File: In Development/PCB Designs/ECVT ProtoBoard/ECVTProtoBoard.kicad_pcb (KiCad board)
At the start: 2 copper layers, 28 parts, among them J1 Motor Driver, J10 Conn_01x08, J11 5V, J12 Hall Effect, J13 Hall Effect, J14 External Power Switch, J15 Conn_01x08, J16 MotorDriver2, J18 3V3, J19 GND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

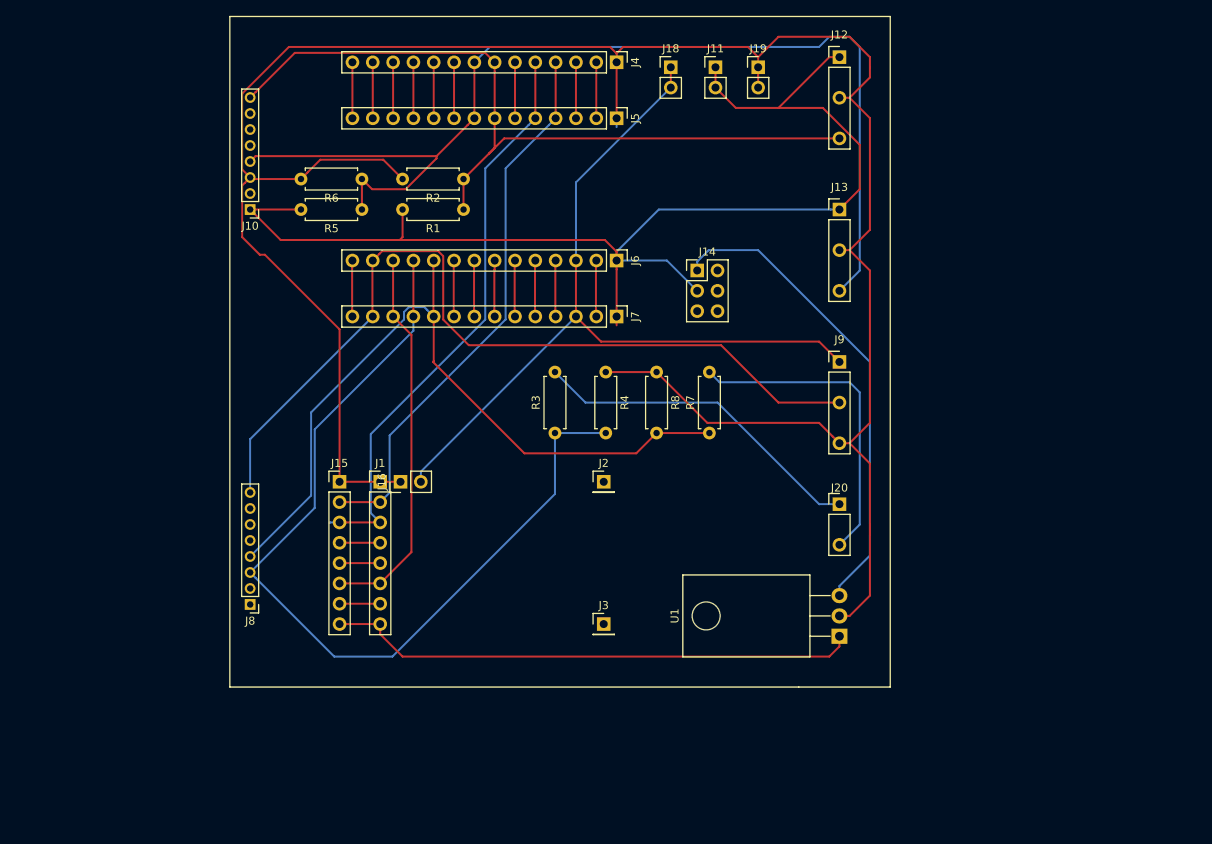
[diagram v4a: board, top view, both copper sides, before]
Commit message: Fixed edge cuts on DAQ PCB
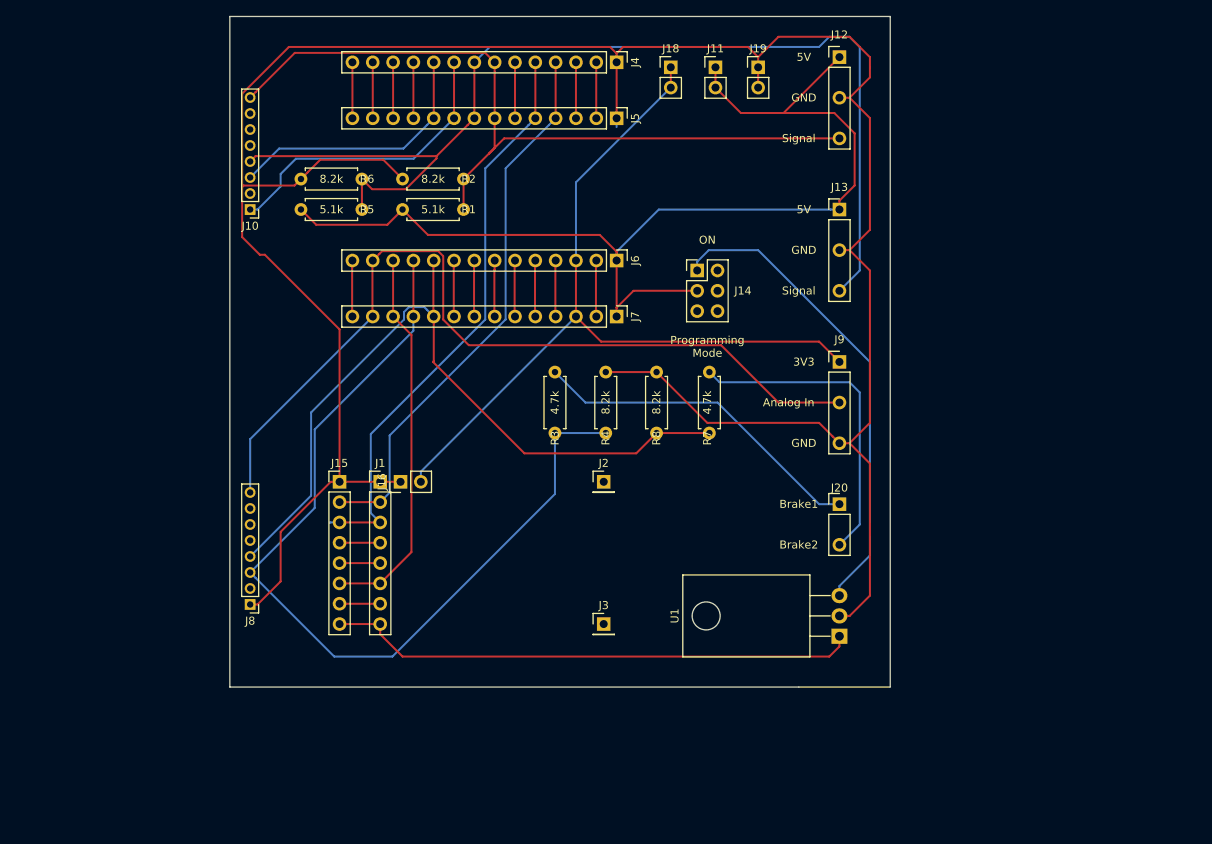
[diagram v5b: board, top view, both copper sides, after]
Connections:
- J10 pad 3: Net-(J1-Pad1) -> Net-(J10-Pad3)
- J11 pad 1: Net-(J10-Pad1) -> Net-(J11-Pad1)
- J11 pad 2: Net-(J10-Pad1) -> Net-(J11-Pad1)
- J12 pad 1: Net-(J10-Pad1) -> Net-(J11-Pad1)
- J13 pad 1: Net-(J10-Pad1) -> Net-(J11-Pad1)
- J14 pad 3: Net-(J10-Pad1) -> Net-(J11-Pad1)
- J4 pad 10: Net-(J4-Pad10) -> Net-(J10-Pad3)
- J4 pad 9: Net-(J4-Pad9) -> Net-(J10-Pad1)
- J5 pad 10: Net-(J4-Pad10) -> Net-(J10-Pad3)
- J5 pad 9: Net-(J4-Pad9) -> Net-(J10-Pad1)
- J6 pad 1: Net-(J10-Pad1) -> Net-(J11-Pad1)
- J7 pad 1: Net-(J10-Pad1) -> Net-(J11-Pad1)
- J8 pad 1: Net-(J1-Pad6) -> Net-(J1-Pad1)
- R1 pad 2: Net-(J10-Pad1) -> Net-(J11-Pad1)
- R5 pad 2: Net-(J10-Pad1) -> Net-(J11-Pad1)
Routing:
- net Net-(J11-Pad1): track 0.00 -> 135.9 mm
- net Net-(J10-Pad1): track 153.2 -> 38.1 mm
- net Net-(J10-Pad3): track 0.00 -> 33.0 mm
- net Net-(J1-Pad1): track 297.2 -> 318.8 mm
- net Net-(J4-Pad9): track 7.00 -> 0.00 mm
- net Net-(J4-Pad10): track 7.00 -> 0.00 mm
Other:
- board outline added: 82.6 x 83.8 mm
- board text added: "3V3"
- board text added: "4.7k"
- board text added: "5.1k"
- board text added: "5V"
- board text added: "8.2k"
- board text added: "Analog In"
- board text added: "Brake1"
- board text added: "Brake2"
- board text added: "GND"
- board text added: "ON"
- board text added: "Programming Mode"
- board text added: "Signal"

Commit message: Finished DAQ and eCVT PCBs rev 2.1. Ready for ordering from JLCPCB
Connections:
- J12 pad 3: Net-(J10-Pad8) -> Net-(J10-Pad1)
- J13 pad 3: Net-(J10-Pad4) -> Net-(J10-Pad3)
- J4 pad 10: Net-(J10-Pad3) -> Net-(J10-Pad8)
- J4 pad 7: Net-(J10-Pad8) -> Net-(J10-Pad1)
- J4 pad 8: Net-(J10-Pad4) -> Net-(J10-Pad3)
- J4 pad 9: Net-(J10-Pad1) -> Net-(J10-Pad4)
- J5 pad 10: Net-(J10-Pad3) -> Net-(J10-Pad8)
- J5 pad 7: Net-(J10-Pad8) -> Net-(J10-Pad1)
- J5 pad 8: Net-(J10-Pad4) -> Net-(J10-Pad3)
- J5 pad 9: Net-(J10-Pad1) -> Net-(J10-Pad4)
- J8 pad 3: Net-(J6-Pad11) -> Net-(J6-Pad10)
- J8 pad 4: Net-(J6-Pad10) -> Net-(J6-Pad11)
- R1 pad 1: Net-(J10-Pad8) -> Net-(J10-Pad1)
- R2 pad 1: Net-(J10-Pad8) -> Net-(J10-Pad1)
- R3 pad 2: Net-(J20-Pad1) -> Net-(J20-Pad2)
- R5 pad 1: Net-(J10-Pad4) -> Net-(J10-Pad3)
- R6 pad 1: Net-(J10-Pad4) -> Net-(J10-Pad3)
- R7 pad 2: Net-(J20-Pad2) -> Net-(J20-Pad1)
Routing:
- net Net-(J10-Pad3): track 33.0 -> 140.8 mm
- net Net-(J10-Pad4): track 134.4 -> 34.7 mm
- net Net-(J10-Pad1): track 38.1 -> 103.5 mm
- net Net-(J10-Pad8): track 98.0 -> 33.4 mm
- net Net-(J16-Pad2): track 100.0 -> 145.7 mm
- net Net-(J6-Pad13): track 106.7 -> 145.0 mm
- net Net-(J1-Pad3): track 72.9 -> 110.7 mm
- net Net-(J6-Pad11): track 112.3 -> 76.2 mm
- net Net-(J1-Pad2): track 69.1 -> 102.6 mm
- net Net-(J20-Pad1): track 42.4 -> 24.0 mm
- net Net-(J11-Pad1): track 135.9 -> 152.2 mm
- net Net-(J6-Pad10): track 96.0 -> 109.2 mm
- net Net-(J20-Pad2): track 40.0 -> 45.2 mm
- net Net-(J1-Pad6): track 48.0 -> 53.0 mm
- net Net-(J1-Pad1): track 318.8 -> 322.8 mm
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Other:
- outline, holes or cut-outs redrawn
- board text added: "Georgia Tech"
- board text added: "OFF ROAD"
